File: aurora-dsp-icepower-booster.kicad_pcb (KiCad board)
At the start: 2 copper layers, 200 x 200 mm, 243 parts, among them J1 XLR_IN_1, J10 XLR3_OUT, J11 XLR3_OUT, J12 XLR3_OUT, J13 24V DC, J14 REMOTE 3.5mm, J2 XLR_IN_2, J3 XLR_IN_3, J4 XLR_IN_4, J5 XLR_IN_5, J6 XLR_IN_6, J7 XLR3_OUT, J8 XLR3_OUT, J9 XLR3_OUT, SW1 Gain CH1, SW2 Gain CH2, SW3 Gain CH3, SW4 Gain CH4, SW5 Gain CH5, SW6 Gain CH6, SW7 ALWAYS/REMOTE, U1 LM4562, U10 LM4562, U11 LM4562, U12 LM4562, U13 TEL5-2422, U14 ADP7118ARDZ-11, U15 ADP7182AUJZ-11, U2 LM4562, U3 LM4562, U4 LM4562, U5 LM4562, U6 LM4562, U7 LM4562, U8 LM4562, U9 LM4562

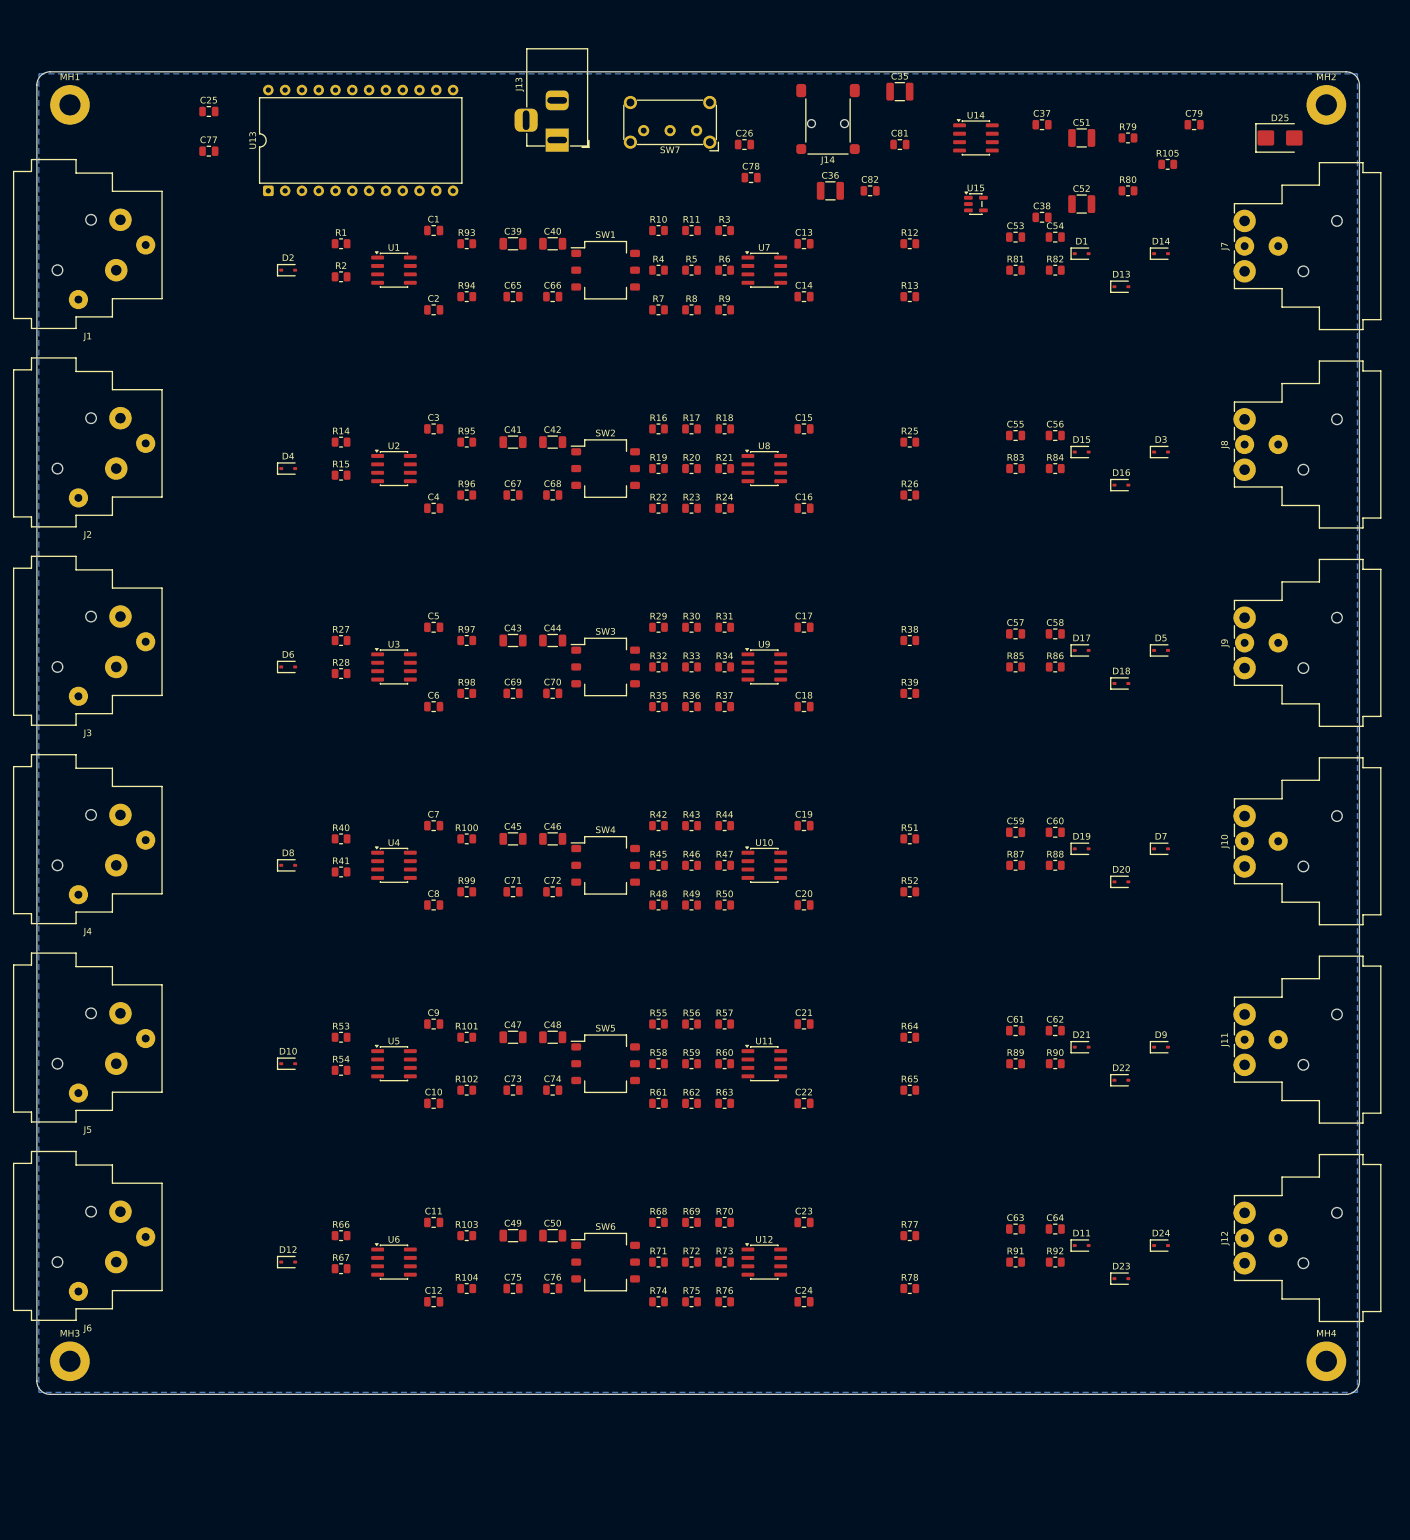
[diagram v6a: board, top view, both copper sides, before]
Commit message: PCB: V+/V- Power Bus Routing (B.Cu Trunks x=67/69/117/119, F.Cu Stubs, 104 Tracks + 39 Vias, 0 Shorts)
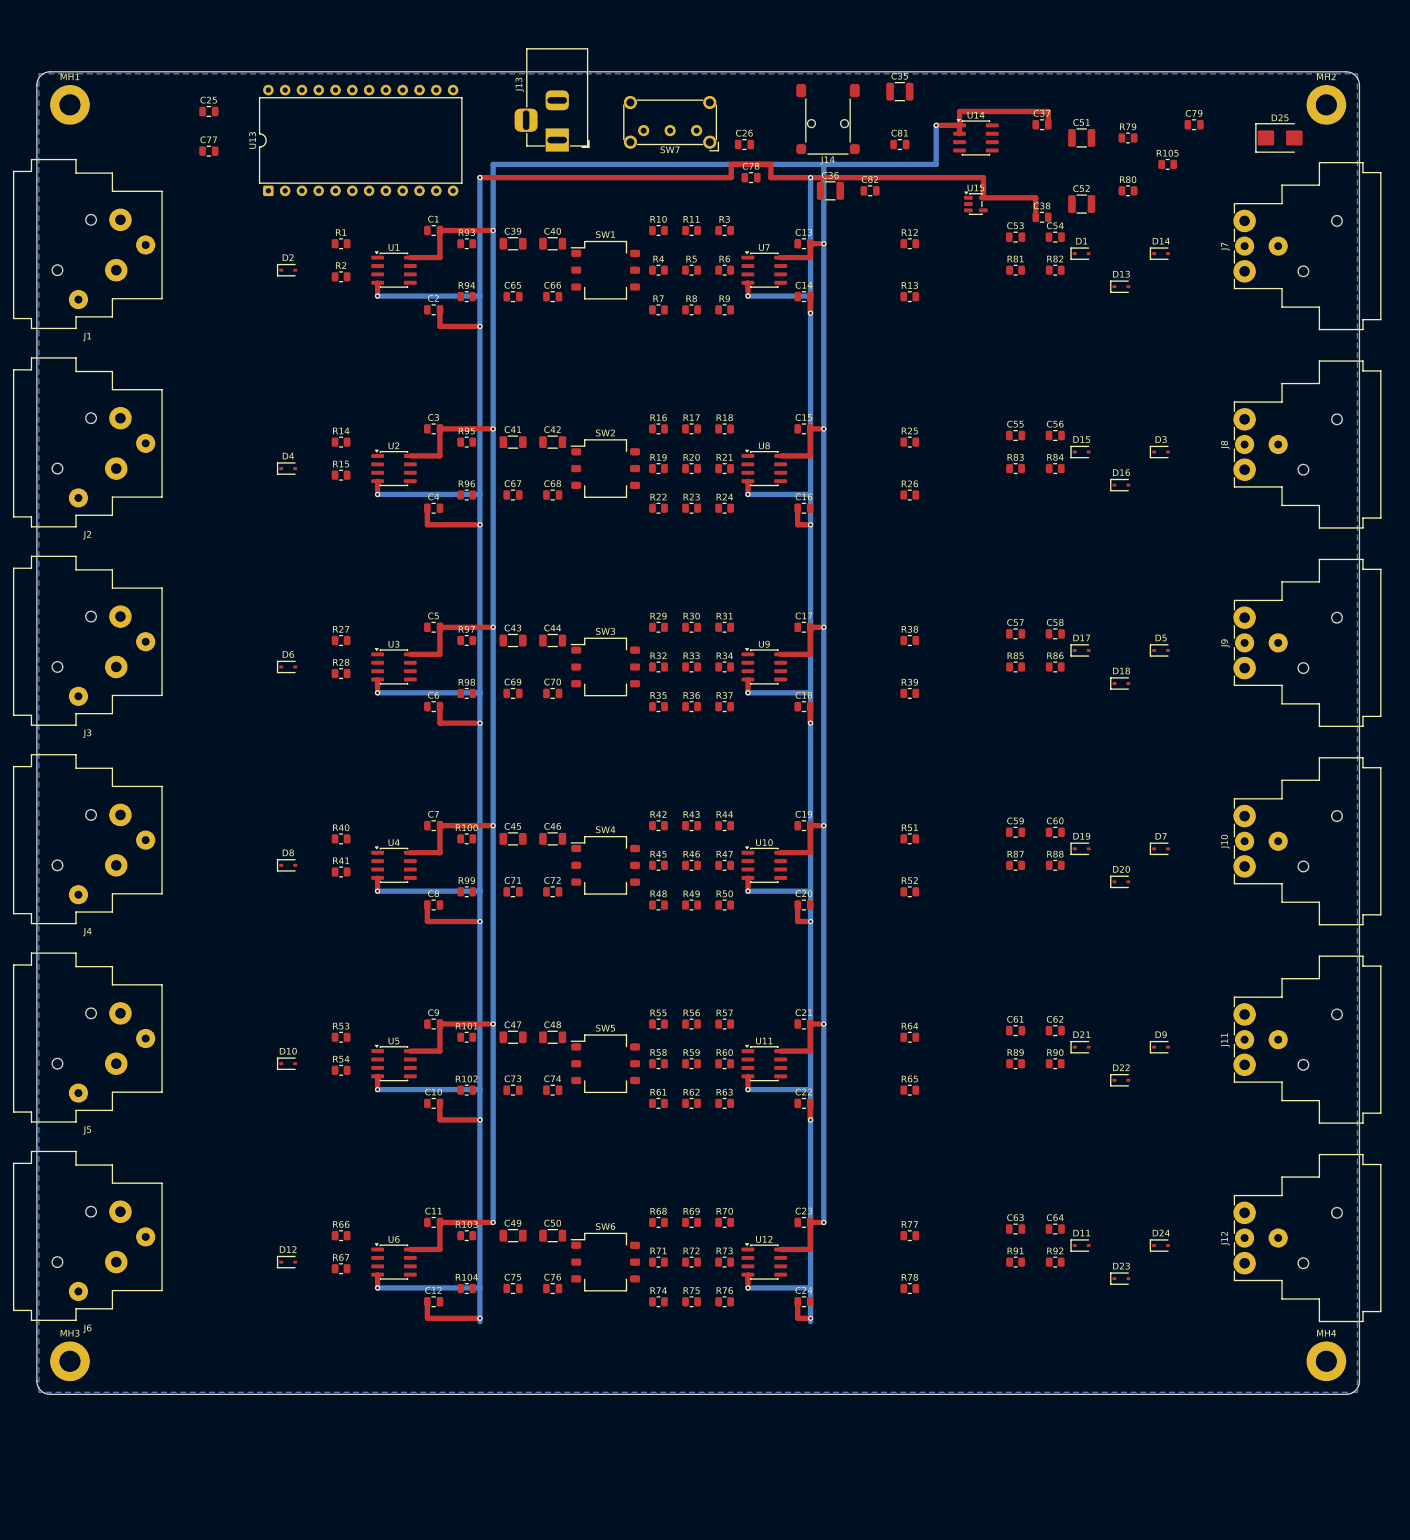
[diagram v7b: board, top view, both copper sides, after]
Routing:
- net /V-: track 0.00 -> 691.8 mm, vias 0 -> 26
- net /V+: track 0.00 -> 576.6 mm, vias 0 -> 13

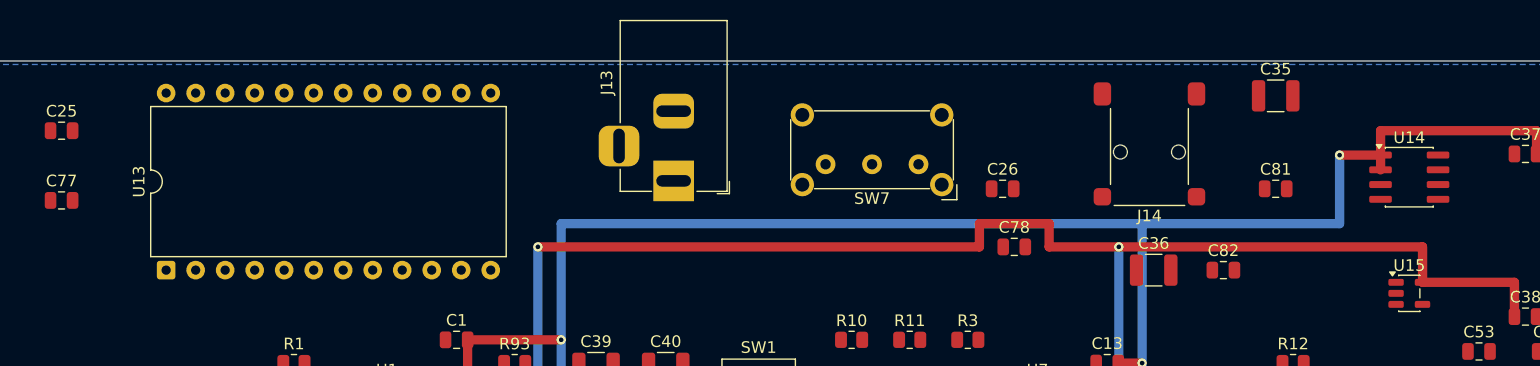
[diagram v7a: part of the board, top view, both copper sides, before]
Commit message: PCB: +12V/-12V/+24V_IN Routing (39 Tracks + 6 Vias, B.Cu Bridges, 0 Shorts)
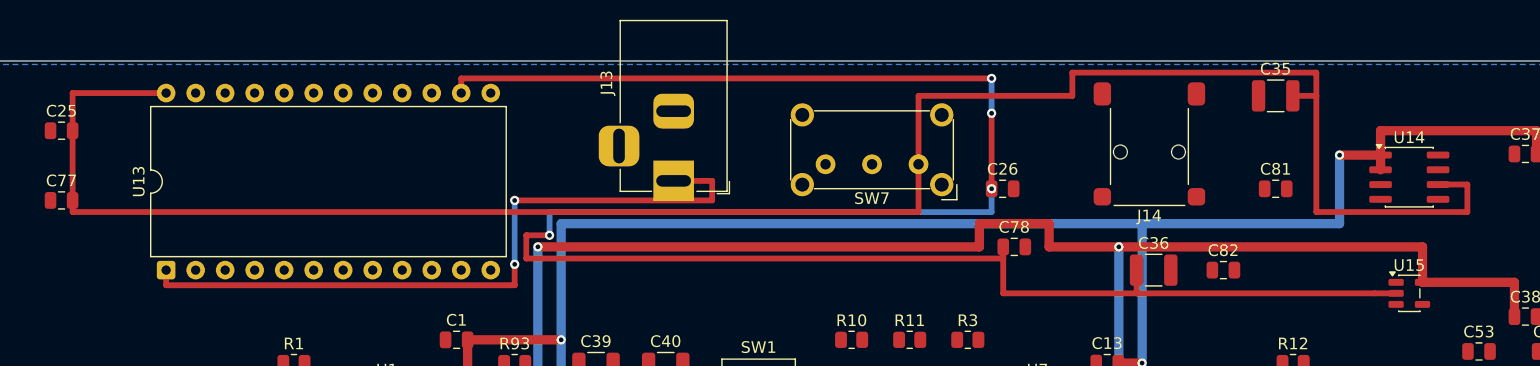
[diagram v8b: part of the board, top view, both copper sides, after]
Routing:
- net /-12V: track 0.00 -> 184.3 mm, vias 0 -> 4
- net /+12V: track 0.00 -> 169.3 mm
- net /+24V_IN: track 0.00 -> 60.6 mm, vias 0 -> 2
